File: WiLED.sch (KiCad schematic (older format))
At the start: 28 parts, among them J1 USB 3V En, P1 DC In, P2 LED Connector, P3 Serial to USB, P4 ADAFRUIT_FEATHER, Q1 BC548, Q2 BC548, SW1 Reset, SW2 Bootload, U1 ESP-12, U3 R-78E-0.5

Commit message: Removed auto-reset circuit
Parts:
- removed J1: USB 3V En, Buttons_Switches_SMD:SW_SPST_SKQG, symbol Jumper_NO_Small
- removed Q1, Q2: BC548, TO_SOT_Packages_SMD:SOT-23_Handsoldering, symbol Q_NPN_CBE
- removed R10, R9: 10k, Resistors_SMD:R_0603_HandSoldering, symbol R
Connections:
- net labels removed: CTS, DTR
- wire segments 124 -> 102
- no-connect marks 15 -> 18
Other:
- note added: "Serial to USB Header"
- note removed: "Serial to USB Header, auto-reset"
- moved on the sheet: C4, C5, D1, P3, R11, R?

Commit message: Final draft
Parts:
- R1, R2, R3, R4, R5: footprint Resistors_SMD:R_0603_HandSoldering -> Resistors_SMD:R_0805_HandSoldering
- R6, R7: renamed from R?; footprint Resistors_SMD:R_0603_HandSoldering -> Resistors_SMD:R_0805_HandSoldering
- R8: renamed from R11; footprint Resistors_SMD:R_0603_HandSoldering -> Resistors_SMD:R_0805_HandSoldering
- SW1, SW2: footprint Buttons_Switches_SMD:SW_SPST_SKQG -> Buttons_Switches_THT:SW_PUSH_6mm
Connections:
- net GND: now also P1.1; no longer P1.2
- net RAW: now also P1.2; no longer P1.1
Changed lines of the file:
@@
 Sheet 1 1
 Title "WiLED ESP-12 Feather"
-Date "2017-09-07"
-Rev "0.3"
+Date "2017-09-10"
+Rev "1.0"
 Comp "Sean Lanigan"
 Comment1 "Requires RF69 Featherwing to connect to low-power radio network."
 Comment2 "Main ESP-12 based Feather compatible board for the WiLED Lamp."
 Comment3 ""
-Comment4 ""
+Comment4 "Released under the CERN Open Hardware Licence v1.2"
 $EndDescr
 $Comp
@@
 F 0 "R2" V 9180 1350 50  0000 C CNN
 F 1 "10k" V 9100 1350 50  0000 C CNN
-F 2 "Resistors_SMD:R_0603_HandSoldering" V 9030 1350 50  0001 C CNN
+F 2 "Resistors_SMD:R_0805_HandSoldering" V 9030 1350 50  0001 C CNN
 F 3 "" H 9100 1350 50  0000 C CNN
 	1    9100 1350
@@
 F 0 "R1" V 8630 1350 50  0000 C CNN
 F 1 "10k" V 8550 1350 50  0000 C CNN
-F 2 "Resistors_SMD:R_0603_HandSoldering" V 8480 1350 50  0001 C CNN
+F 2 "Resistors_SMD:R_0805_HandSoldering" V 8480 1350 50  0001 C CNN
 F 3 "" H 8550 1350 50  0000 C CNN
 	1    8550 1350
@@
 F 0 "SW2" H 10200 1780 50  0000 C CNN
 F 1 "Bootload" H 10210 1640 50  0000 C CNN
-F 2 "Buttons_Switches_SMD:SW_SPST_SKQG" H 10200 1700 50  0001 C CNN
+F 2 "Buttons_Switches_THT:SW_PUSH_6mm" H 10200 1700 50  0001 C CNN
 F 3 "" H 10200 1700 50  0000 C CNN
 	1    10200 1700
@@
 F 0 "SW1" H 8550 1780 50  0000 C CNN
 F 1 "Reset" H 8560 1640 50  0000 C CNN
-F 2 "Buttons_Switches_SMD:SW_SPST_SKQG" H 8550 1700 50  0001 C CNN
+F 2 "Buttons_Switches_THT:SW_PUSH_6mm" H 8550 1700 50  0001 C CNN
 F 3 "" H 8550 1700 50  0000 C CNN
 	1    8550 1700
@@
 F 0 "R5" V 10830 1650 50  0000 C CNN
 F 1 "10k" V 10750 1650 50  0000 C CNN
-F 2 "Resistors_SMD:R_0603_HandSoldering" V 10680 1650 50  0001 C CNN
+F 2 "Resistors_SMD:R_0805_HandSoldering" V 10680 1650 50  0001 C CNN
 F 3 "" H 10750 1650 50  0000 C CNN
 	1    10750 1650
@@
 F 0 "R3" V 9730 1350 50  0000 C CNN
 F 1 "10k" V 9650 1350 50  0000 C CNN
-F 2 "Resistors_SMD:R_0603_HandSoldering" V 9580 1350 50  0001 C CNN
+F 2 "Resistors_SMD:R_0805_HandSoldering" V 9580 1350 50  0001 C CNN
 F 3 "" H 9650 1350 50  0000 C CNN
 	1    9650 1350
@@
 F 0 "R4" V 10280 1350 50  0000 C CNN
 F 1 "10k" V 10200 1350 50  0000 C CNN
-F 2 "Resistors_SMD:R_0603_HandSoldering" V 10130 1350 50  0001 C CNN
+F 2 "Resistors_SMD:R_0805_HandSoldering" V 10130 1350 50  0001 C CNN
 F 3 "" H 10200 1350 50  0000 C CNN
 	1    10200 1350
@@
 F 3 "" H 8525 2950 50  0001 C CNN
 	1    8550 2950
-	1    0    0    -1
+	1    0    0    1
 $EndComp
 Text GLabel 9150 2600 1    47   Input ~ 0
@@
 $EndComp
 $Comp
-L GND #PWR018
+L GND #PWR016
 U 1 1 59982D30
 P 6550 4350
-F 0 "#PWR018" H 6550 4100 50  0001 C CNN
+F 0 "#PWR016" H 6550 4100 50  0001 C CNN
 F 1 "GND" H 6550 4200 50  0000 C CNN
 F 2 "" H 6550 4350 50  0000 C CNN
@@
 $EndComp
 $Comp
-L GND #PWR020
+L GND #PWR017
 U 1 1 5998304D
 P 7400 4350
-F 0 "#PWR020" H 7400 4100 50  0001 C CNN
+F 0 "#PWR017" H 7400 4100 50  0001 C CNN
 F 1 "GND" H 7400 4200 50  0000 C CNN
 F 2 "" H 7400 4350 50  0000 C CNN
@@
 $EndComp
 $Comp
-L GND #PWR021
+L GND #PWR018
 U 1 1 5999AA51
 P 6650 1800
-F 0 "#PWR021" H 6650 1550 50  0001 C CNN
+F 0 "#PWR018" H 6650 1550 50  0001 C CNN
 F 1 "GND" H 6650 1650 50  0000 C CNN
 F 2 "" H 6650 1800 50  0000 C CNN
@@
 Power LED
 $Comp
-L +3.3V #PWR025
+L +3.3V #PWR019
 U 1 1 59B07E62
 P 5800 2800
-F 0 "#PWR025" H 5800 2650 50  0001 C CNN
+F 0 "#PWR019" H 5800 2650 50  0001 C CNN
 F 1 "+3.3V" H 5800 2940 50  0000 C CNN
 F 2 "" H 5800 2800 50  0000 C CNN
@@
 $EndComp
 $Comp
-L GND #PWR026
+L GND #PWR020
 U 1 1 59B08869
 P 7200 3050
-F 0 "#PWR026" H 7200 2800 50  0001 C CNN
+F 0 "#PWR020" H 7200 2800 50  0001 C CNN
 F 1 "GND" H 7200 2900 50  0000 C CNN
 F 2 "" H 7200 3050 50  0000 C CNN
@@
 $EndComp
 $Comp
-L R R11
+L R R8
 U 1 1 59B0899F
 P 6850 2900
-F 0 "R11" V 6750 2900 50  0000 C CNN
+F 0 "R8" V 6750 2900 50  0000 C CNN
 F 1 "1k" V 6850 2900 50  0000 C CNN
-F 2 "Resistors_SMD:R_0603_HandSoldering" V 6780 2900 50  0001 C CNN
+F 2 "Resistors_SMD:R_0805_HandSoldering" V 6780 2900 50  0001 C CNN
 F 3 "" H 6850 2900 50  0000 C CNN
 	1    6850 2900
@@
 ENC_SW
 $Comp
-L +3.3V #PWR029
+L +3.3V #PWR021
 U 1 1 59B0DF7F
 P 5750 3900
-F 0 "#PWR029" H 5750 3750 50  0001 C CNN
+F 0 "#PWR021" H 5750 3750 50  0001 C CNN
 F 1 "+3.3V" H 5750 4040 50  0000 C CNN
 F 2 "" H 5750 3900 50  0000 C CNN
@@
 $EndComp
 $Comp
-L GND #PWR030
+L GND #PWR022
 U 1 1 59B10828
 P 5750 4700
-F 0 "#PWR030" H 5750 4450 50  0001 C CNN
+F 0 "#PWR022" H 5750 4450 50  0001 C CNN
 F 1 "GND" H 5750 4550 50  0000 C CNN
 F 2 "" H 5750 4700 50  0000 C CNN
@@
 	1700 2250 1750 2250
 $Comp
-L R R?
+L R R6
 U 1 1 59B14401
 P 5750 4100
-F 0 "R?" V 5830 4100 50  0000 C CNN
+F 0 "R6" V 5830 4100 50  0000 C CNN
 F 1 "2.7k" V 5750 4100 50  0000 C CNN
-F 2 "Resistors_SMD:R_0603_HandSoldering" V 5680 4100 50  0001 C CNN
+F 2 "Resistors_SMD:R_0805_HandSoldering" V 5680 4100 50  0001 C CNN
 F 3 "" H 5750 4100 50  0000 C CNN
 	1    5750 4100
@@
 	5750 3900 5750 3950
 $Comp
-L R R?
+L R R7
 U 1 1 59B14844
 P 5750 4500
-F 0 "R?" V 5830 4500 50  0000 C CNN
+F 0 "R7" V 5830 4500 50  0000 C CNN
 F 1 "1k" V 5750 4500 50  0000 C CNN
-F 2 "Resistors_SMD:R_0603_HandSoldering" V 5680 4500 50  0001 C CNN
+F 2 "Resistors_SMD:R_0805_HandSoldering" V 5680 4500 50  0001 C CNN
 F 3 "" H 5750 4500 50  0000 C CNN
 	1    5750 4500
@@
 	5150 900  5150 2100
 $Comp
-L GND #PWR?
+L GND #PWR023
 U 1 1 59B4D73F
 P 3000 5500
-F 0 "#PWR?" H 3000 5250 50  0001 C CNN
+F 0 "#PWR023" H 3000 5250 50  0001 C CNN
 F 1 "GND" H 3000 5350 50  0000 C CNN
 F 2 "" H 3000 5500 50  0000 C CNN

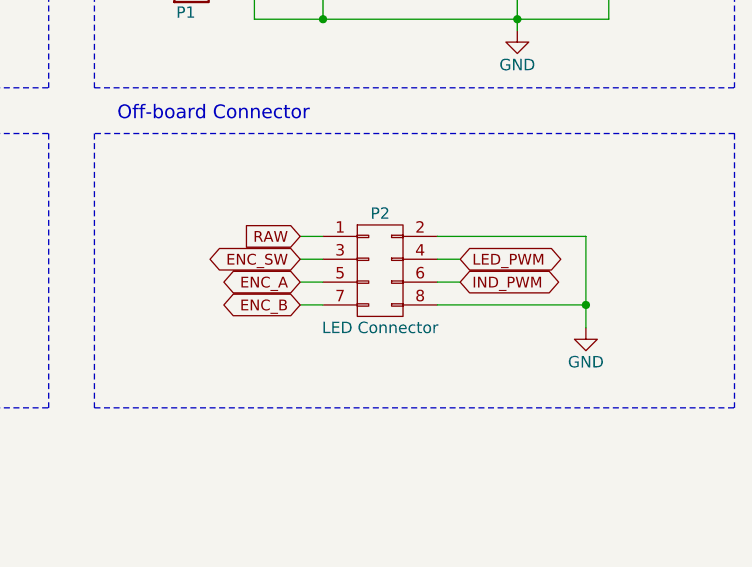
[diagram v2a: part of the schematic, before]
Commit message: Change LED_PWM and IND_PWM for better routing
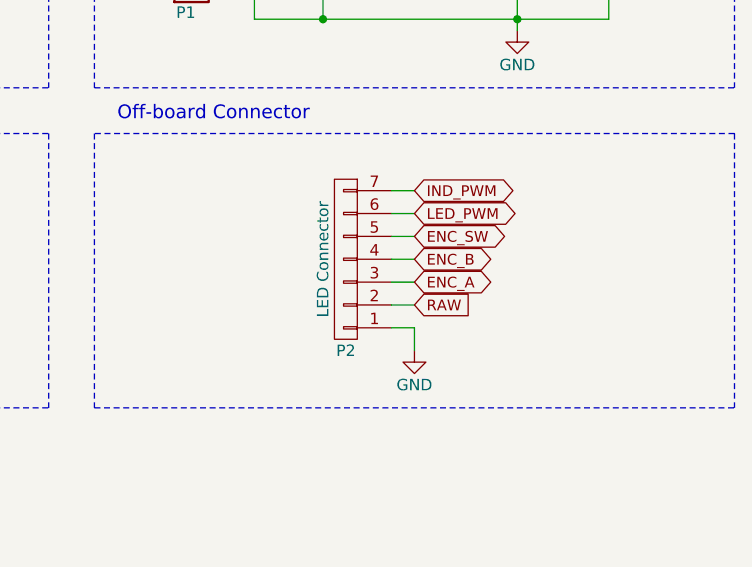
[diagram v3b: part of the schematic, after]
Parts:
- removed P2: LED Connector, Pin_Headers:Pin_Header_Straight_2x04, symbol CONN_02X04
- added P2: LED Connector, custom-footprints:7x2mm, symbol CONN_01X07
- C3, C4, C5: footprint Capacitors_SMD:C_0603_HandSoldering -> Capacitors_SMD:C_0805_HandSoldering
- P1: footprint custom-footprints:Terminal -> custom-footprints:2x2mm
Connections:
- net 0: now also P2.3 (P3)
- net 2: now also P2.4 (P4)
- net ENC_SW: now also P2.5 (P5)
- net GND: now also P2.1 (P1)
- net IND_PWM: now also P2.7 (P7)
- net LED_PWM: now also P2.6 (P6)
- net RAW: now also P2.2 (P2)
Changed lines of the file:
@@
 F 0 "C3" V 2250 1150 50  0000 L CNN
 F 1 "100nF" V 2500 1150 50  0000 L CNN
-F 2 "Capacitors_SMD:C_0603_HandSoldering" H 2388 1150 50  0001 C CNN
+F 2 "Capacitors_SMD:C_0805_HandSoldering" H 2388 1150 50  0001 C CNN
 F 3 "" H 2350 1300 50  0000 C CNN
 	1    2350 1300
@@
 F 0 "P1" H 8550 3200 50  0000 C TNN
 F 1 "DC In" V 8400 2950 50  0000 C TNN
-F 2 "custom-footprints:Terminal" H 8550 2725 50  0001 C CNN
+F 2 "custom-footprints:2x2mm" H 8550 2725 50  0001 C CNN
 F 3 "" H 8525 2950 50  0001 C CNN
 	1    8550 2950
@@
 Text GLabel 3550 4700 0    47   Input ~ 0
 RAW
-$Comp
-L CONN_02X04 P2
-U 1 1 59979E35
-P 9400 4300
-F 0 "P2" H 9400 4550 50  0000 C CNN
-F 1 "LED Connector" H 9400 4050 50  0000 C CNN
-F 2 "Pin_Headers:Pin_Header_Straight_2x04" H 9400 3100 50  0001 C CNN
-F 3 "" H 9400 3100 50  0000 C CNN
-	1    9400 4300
-	1    0    0    -1
-$EndComp
-Text GLabel 9050 4150 0    47   Input ~ 0
+Text GLabel 9550 4450 2    47   Input ~ 0
 RAW
 $Comp
 L GND #PWR015
 U 1 1 5997B5E9
-P 10300 4550
-F 0 "#PWR015" H 10300 4300 50  0001 C CNN
-F 1 "GND" H 10300 4400 50  0000 C CNN
-F 2 "" H 10300 4550 50  0000 C CNN
-F 3 "" H 10300 4550 50  0000 C CNN
-	1    10300 4550
-	1    0    0    -1
-$EndComp
-Text GLabel 9750 4250 2    47   BiDi ~ 0
+P 9550 4650
+F 0 "#PWR015" H 9550 4400 50  0001 C CNN
+F 1 "GND" H 9550 4500 50  0000 C CNN
+F 2 "" H 9550 4650 50  0000 C CNN
+F 3 "" H 9550 4650 50  0000 C CNN
+	1    9550 4650
+	1    0    0    -1
+$EndComp
+Text GLabel 9550 4050 2    47   BiDi ~ 0
 LED_PWM
 Text GLabel 3800 2350 2    47   BiDi ~ 0
@@
 Text GLabel 3800 2550 2    47   BiDi ~ 0
 ENC_B
-Text GLabel 9050 4350 0    47   BiDi ~ 0
+Text GLabel 9550 4350 2    47   BiDi ~ 0
 ENC_A
-Text GLabel 9050 4450 0    47   BiDi ~ 0
+Text GLabel 9550 4250 2    47   BiDi ~ 0
 ENC_B
-Text GLabel 9050 4250 0    47   BiDi ~ 0
+Text GLabel 9550 4150 2    47   BiDi ~ 0
 ENC_SW
-Text GLabel 9750 4350 2    47   BiDi ~ 0
+Text GLabel 9550 3950 2    47   BiDi ~ 0
 IND_PWM
 Text Notes 8250 3650 0    60   ~ 0
@@
 F 0 "C4" H 6575 4250 50  0000 L CNN
 F 1 "100nF" H 6575 4050 50  0000 L CNN
-F 2 "Capacitors_SMD:C_0603_HandSoldering" H 6588 4000 50  0001 C CNN
+F 2 "Capacitors_SMD:C_0805_HandSoldering" H 6588 4000 50  0001 C CNN
 F 3 "" H 6550 4150 50  0000 C CNN
 	1    6550 4150
@@
 F 0 "C5" H 7425 4250 50  0000 L CNN
 F 1 "100nF" H 7425 4050 50  0000 L CNN
-F 2 "Capacitors_SMD:C_0603_HandSoldering" H 7438 4000 50  0001 C CNN
+F 2 "Capacitors_SMD:C_0805_HandSoldering" H 7438 4000 50  0001 C CNN
 F 3 "" H 7400 4150 50  0000 C CNN
 	1    7400 4150
@@
 Wire Wire Line
 	3550 4700 3650 4700
-Wire Wire Line
-	9650 4150 10300 4150
-Wire Wire Line
-	9050 4150 9150 4150
-Wire Wire Line
-	9050 4250 9150 4250
-Wire Wire Line
-	9050 4350 9150 4350
-Wire Wire Line
-	9050 4450 9150 4450
-Wire Wire Line
-	10300 4150 10300 4550
-Wire Wire Line
-	9650 4250 9750 4250
-Wire Wire Line
-	9750 4350 9650 4350
 Wire Notes Line
 	10950 3700 10950 4900
@@
 Wire Notes Line
 	700  3500 700  900
-Wire Wire Line
-	10300 4450 9650 4450
-Connection ~ 10300 4450
 Text Notes 5250 2250 0    60   ~ 0
 Power LED
@@
 Wire Wire Line
 	3000 5400 3000 5500
+$Comp
+L CONN_01X07 P2
+U 1 1 59B5296F
+P 9250 4250
+F 0 "P2" H 9250 4650 50  0000 C CNN
+F 1 "LED Connector" V 9350 4250 50  0000 C CNN
+F 2 "custom-footprints:7x2mm" H 9250 4250 50  0001 C CNN
+F 3 "" H 9250 4250 50  0000 C CNN
+	1    9250 4250
+	-1   0    0    1
+$EndComp
+Wire Wire Line
+	9450 4550 9550 4550
+Wire Wire Line
+	9550 4550 9550 4650
+Wire Wire Line
+	9450 3950 9550 3950
+Wire Wire Line
+	9450 4050 9550 4050
+Wire Wire Line
+	9450 4150 9550 4150
+Wire Wire Line
+	9450 4250 9550 4250
+Wire Wire Line
+	9450 4350 9550 4350
+Wire Wire Line
+	9450 4450 9550 4450
 $EndSCHEMATC

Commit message: Finalised first draft of PCB
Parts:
- renumbered U3 to U2
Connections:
- net GND: now also P1.2; no longer P1.1
- net RAW: now also P1.1; no longer P1.2
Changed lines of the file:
@@
 $EndComp
 $Comp
-L R-78E-0.5 U3
+L R-78E-0.5 U2
 U 1 1 5996AF16
 P 10000 2700
-F 0 "U3" H 10100 2450 50  0000 C CNN
+F 0 "U2" H 10100 2450 50  0000 C CNN
 F 1 "R-78E-0.5" H 10000 2950 50  0000 C CNN
 F 2 "Power_Integrations:TO-220" H 10000 2700 50  0001 C CNN
@@
 F 3 "" H 8525 2950 50  0001 C CNN
 	1    8550 2950
-	1    0    0    1
+	1    0    0    -1
 $EndComp
 Text GLabel 9150 2600 1    47   Input ~ 0

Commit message: Second draft of PCB
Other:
- note added: "Serial to USB Header (not broken out on PCB)"
- note removed: "Serial to USB Header"
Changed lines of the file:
@@
 RF_CS
 Text Notes 5250 850  0    60   ~ 0
-Serial to USB Header
+Serial to USB Header (not broken out on PCB)
 $Comp
 L CONN_01X06 P3

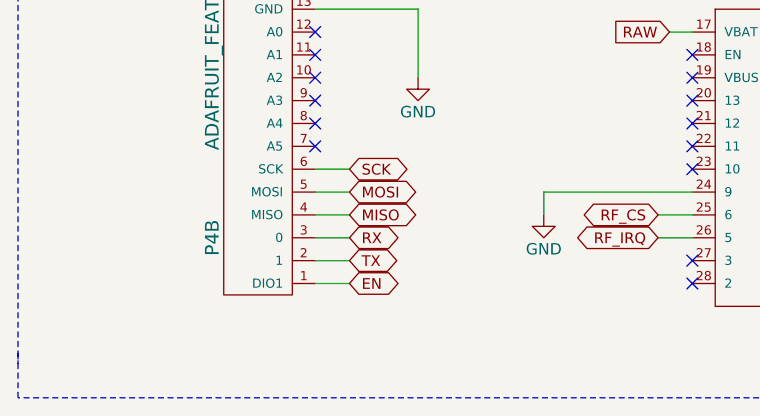
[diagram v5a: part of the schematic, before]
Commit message: Remove EN from DIO1 pin on Feather header
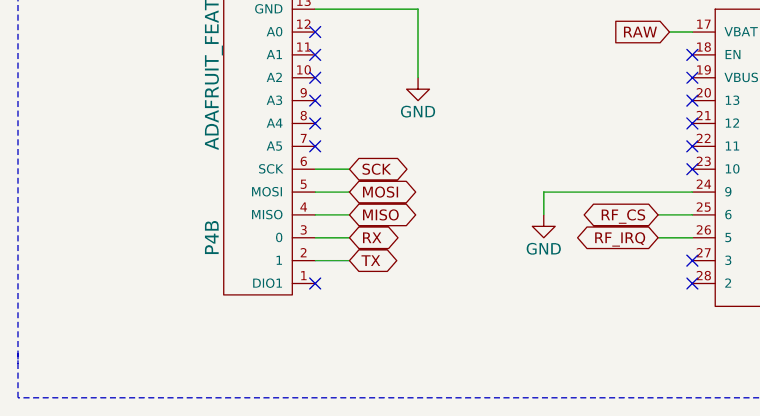
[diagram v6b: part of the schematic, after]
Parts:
- D1: footprint LEDs:LED_0805 -> LEDs:LED-3MM
- L1: footprint Choke_SMD:Choke_SMD_1206_Handsoldering -> custom-footprints:THT_Inductor_small
- P1: footprint custom-footprints:2x2mm -> Connectors_JST:JST_PH_B2B-PH-K_02x2.00mm_Straight
- P2: footprint custom-footprints:7x2mm -> Connectors_JST:JST_PH_B7B-PH-K_07x2.00mm_Straight
- SW1: footprint Buttons_Switches_THT:SW_PUSH_6mm -> custom-footprints:Button_6.5mm
- SW2: footprint Buttons_Switches_THT:SW_PUSH_6mm -> Socket_Strips:Socket_Strip_Straight_1x02
- U2: footprint Power_Integrations:TO-220 -> custom-footprints:Recom_R-78HBxx-0.5
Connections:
- net EN: no longer P4.1 (DIO1)
- no-connect marks 18 -> 19
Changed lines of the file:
@@
 F 0 "SW2" H 10200 1780 50  0000 C CNN
 F 1 "Bootload" H 10210 1640 50  0000 C CNN
-F 2 "Buttons_Switches_THT:SW_PUSH_6mm" H 10200 1700 50  0001 C CNN
+F 2 "Socket_Strips:Socket_Strip_Straight_1x02" H 10200 1700 50  0001 C CNN
 F 3 "" H 10200 1700 50  0000 C CNN
 	1    10200 1700
@@
 F 0 "SW1" H 8550 1780 50  0000 C CNN
 F 1 "Reset" H 8560 1640 50  0000 C CNN
-F 2 "Buttons_Switches_THT:SW_PUSH_6mm" H 8550 1700 50  0001 C CNN
+F 2 "custom-footprints:Button_6.5mm" H 8550 1700 50  0001 C CNN
 F 3 "" H 8550 1700 50  0000 C CNN
 	1    8550 1700
@@
 RX
 Text GLabel 1700 2150 0    47   BiDi ~ 0
-EN
-Text GLabel 2150 5800 2    47   BiDi ~ 0
 EN
 Text GLabel 2100 4300 2    47   BiDi ~ 0
@@
 F 0 "U2" H 10100 2450 50  0000 C CNN
 F 1 "R-78E-0.5" H 10000 2950 50  0000 C CNN
-F 2 "Power_Integrations:TO-220" H 10000 2700 50  0001 C CNN
+F 2 "custom-footprints:Recom_R-78HBxx-0.5" H 10000 2700 50  0001 C CNN
 F 3 "" H 10000 2700 50  0000 C CNN
 	1    10000 2700
@@
 F 0 "L1" V 9400 2700 50  0000 C CNN
 F 1 "3.3uH" V 9525 2700 50  0000 C CNN
-F 2 "Choke_SMD:Choke_SMD_1206_Handsoldering" H 9450 2700 50  0001 C CNN
+F 2 "custom-footprints:THT_Inductor_small" H 9450 2700 50  0001 C CNN
 F 3 "" H 9450 2700 50  0000 C CNN
 	1    9450 2700
@@
 F 0 "P1" H 8550 3200 50  0000 C TNN
 F 1 "DC In" V 8400 2950 50  0000 C TNN
-F 2 "custom-footprints:2x2mm" H 8550 2725 50  0001 C CNN
+F 2 "Connectors_JST:JST_PH_B2B-PH-K_02x2.00mm_Straight" H 8550 2725 50  0001 C CNN
 F 3 "" H 8525 2950 50  0001 C CNN
 	1    8550 2950
@@
 	1700 2050 1750 2050
 Wire Wire Line
-	2000 5800 2150 5800
-Wire Wire Line
 	2450 4400 2450 4150
 Wire Wire Line
@@
 F 0 "D1" H 6200 2800 50  0000 C CNN
 F 1 "Power LED" H 6200 3000 50  0000 C CNN
-F 2 "LEDs:LED_0805" H 6200 2900 50  0001 C CNN
+F 2 "LEDs:LED-3MM" H 6200 2900 50  0001 C CNN
 F 3 "" H 6200 2900 50  0000 C CNN
 	1    6200 2900
@@
 F 0 "P2" H 9250 4650 50  0000 C CNN
 F 1 "LED Connector" V 9350 4250 50  0000 C CNN
-F 2 "custom-footprints:7x2mm" H 9250 4250 50  0001 C CNN
+F 2 "Connectors_JST:JST_PH_B7B-PH-K_07x2.00mm_Straight" H 9250 4250 50  0001 C CNN
 F 3 "" H 9250 4250 50  0000 C CNN
 	1    9250 4250
@@
 Wire Wire Line
 	9450 4450 9550 4450
+NoConn ~ 2000 5800
 $EndSCHEMATC
